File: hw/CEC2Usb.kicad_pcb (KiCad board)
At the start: 2 copper layers, 23.7 x 30.5 mm, 39 parts, among them J1 USB_B_Mini, J2 HDMI_A, J3 HDMI_A, J4 ICSP, Q1 BC817, U1 TLV70233_SOT23-5, U2 ATmega32U2-AU, Y1 16MHz

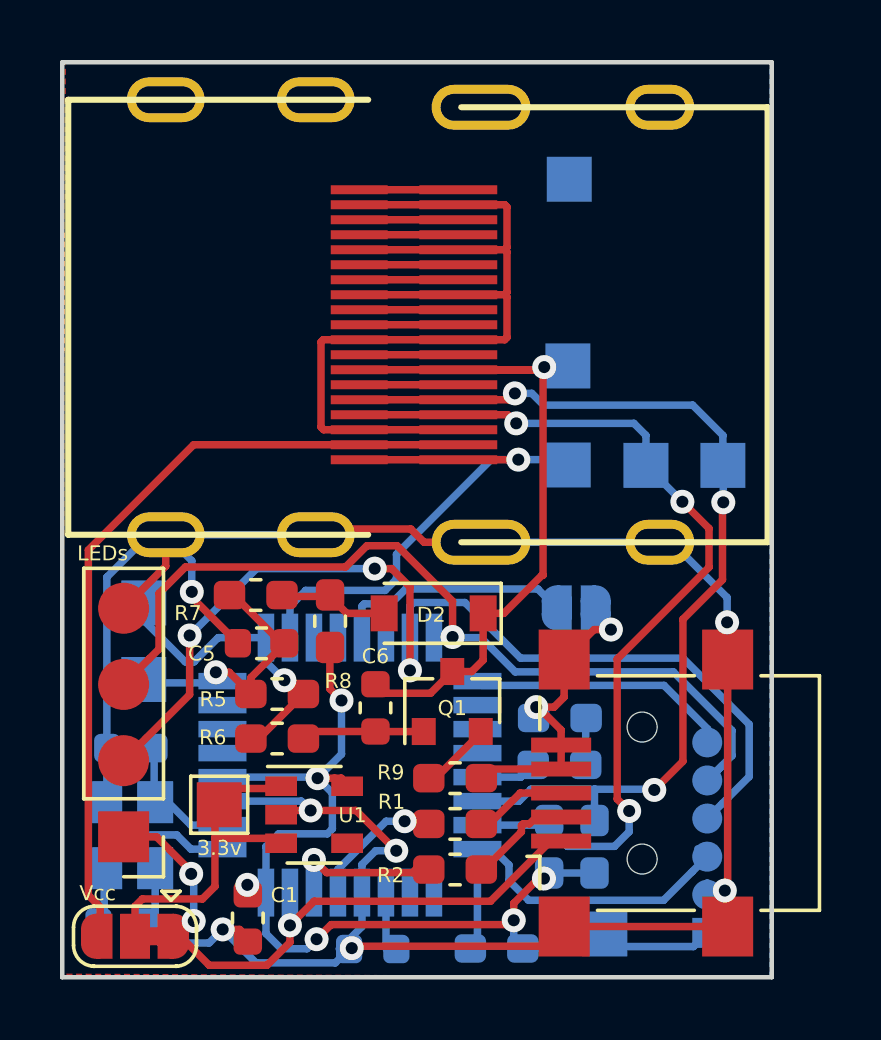
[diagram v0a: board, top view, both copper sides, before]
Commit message: [HW] Minor rev to add reset button to witch to DFU
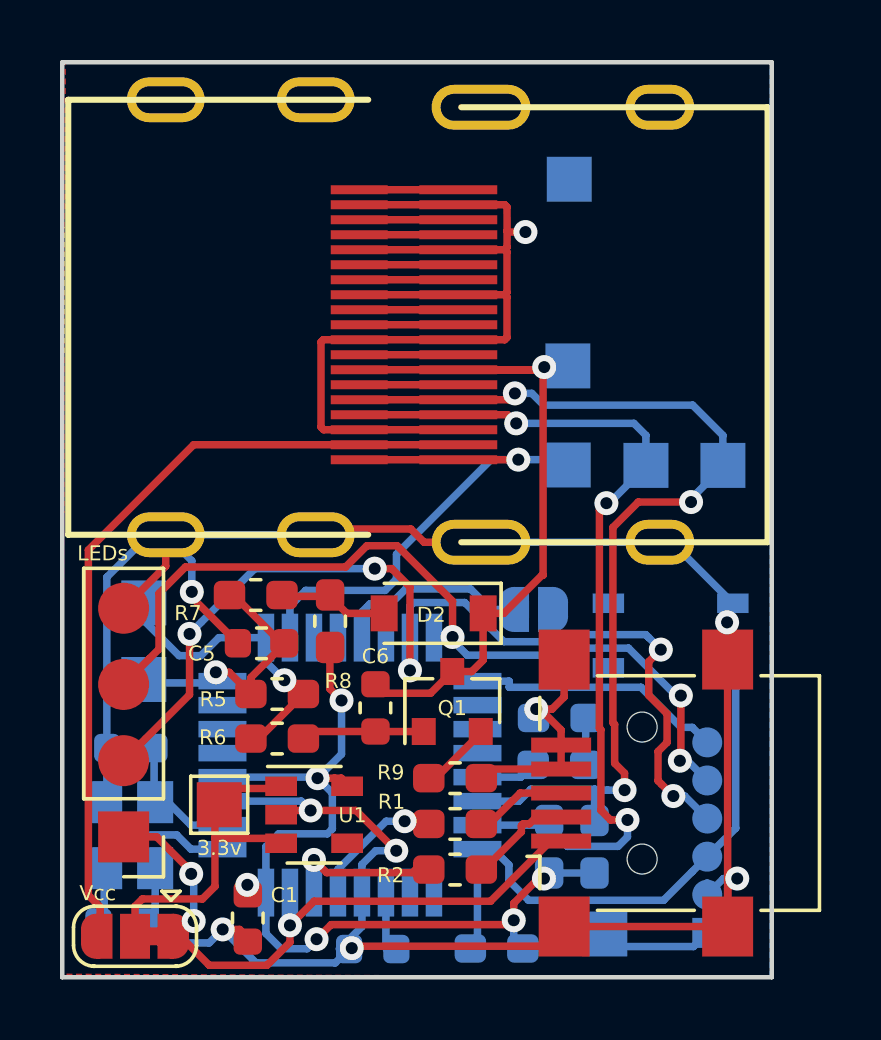
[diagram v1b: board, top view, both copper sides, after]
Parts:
- added Reset: SW_SPST_PTS810, Button_Switch_SMD:SW_SPST_PTS810, B.Cu at (85.4, 63.6)
- moved JP2 1.42 mm to (80.8, 62.7)
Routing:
- net Net-(J4-Pad3): track 13.6 -> 20.0 mm
- net Net-(JP2-Pad1): track 8.04 -> 6.47 mm
- net /SPI_MOSI: track 30.5 -> 29.2 mm, vias 1 -> 3
- net GND: track 133.6 -> 132.4 mm
- net /SDA: track 30.9 -> 30.1 mm
- net /SCL: track 32.7 -> 33.5 mm
- net /SPI_CLK: track 35.3 -> 34.9 mm, vias 3 -> 5
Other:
- board text added: "RedoX 03/2k20 www.redox.ws"
- board text added: "v0.3"
- board text removed: "RedoX 10/2k19 www.redox.ws"
- board text removed: "v0.2"
